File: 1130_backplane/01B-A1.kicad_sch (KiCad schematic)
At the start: 86 parts

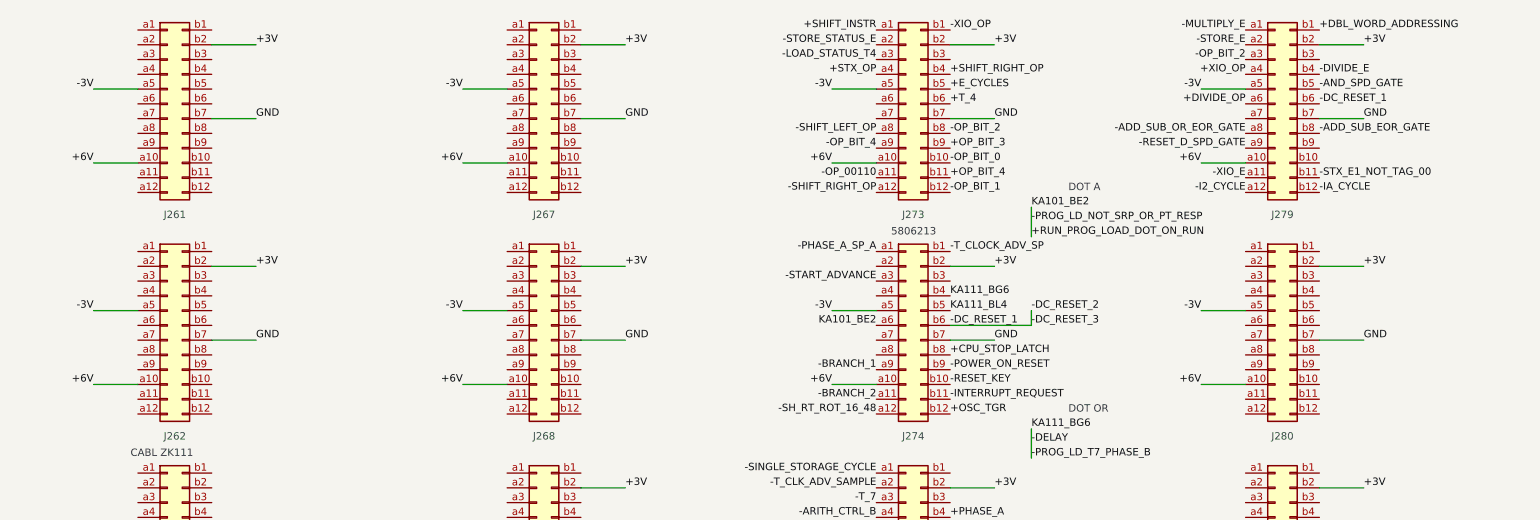
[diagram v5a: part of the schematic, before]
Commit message: Finish page KC101-KC111
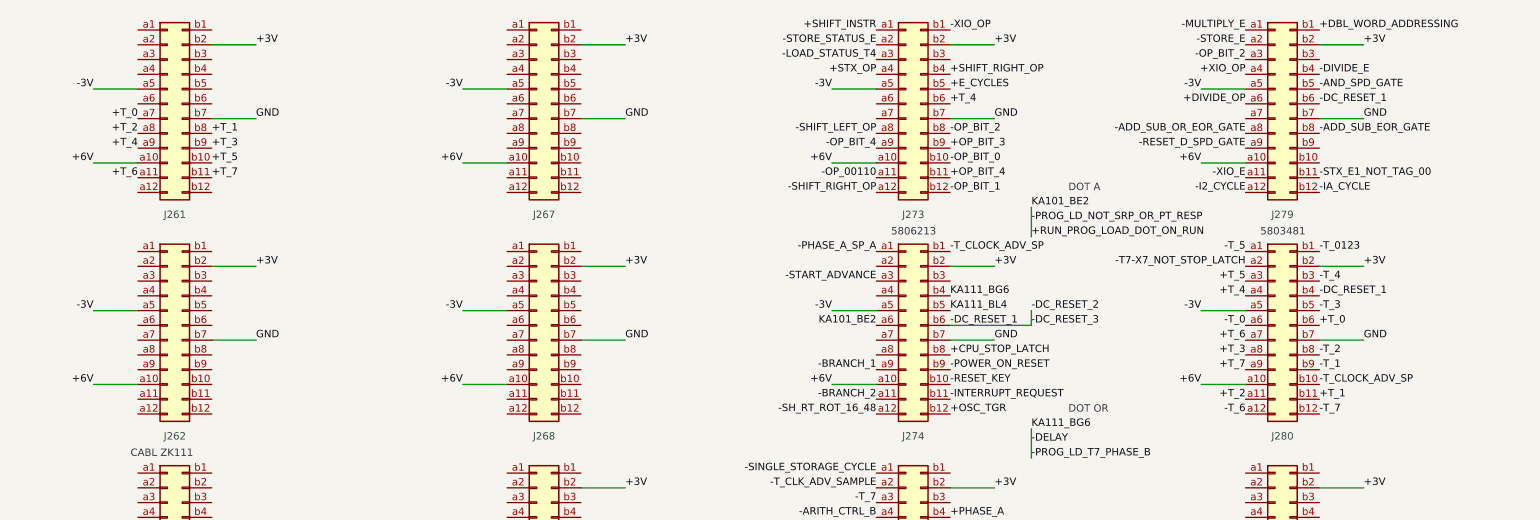
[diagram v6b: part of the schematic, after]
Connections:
- net +T_3: now also J260.b9 (Pin_b9), J279.a8 (Pin_a8)
- net +T_4: now also J260.a9 (Pin_a9), J279.a4 (Pin_a4)
- net +T_5: now also J260.b10 (Pin_b10), J279.a3 (Pin_a3)
- net +T_6: now also J260.a11 (Pin_a11), J279.a7 (Pin_a7)
- net +T_7: now also J260.b11 (Pin_b11), J279.a9 (Pin_a9)
- net -DC_RESET_1: now also J279.b4 (Pin_b4)
- net -T_0: now also J279.a6 (Pin_a6)
- net -T_1: now also J279.b9 (Pin_b9)
- net -T_5: now also J279.a1 (Pin_a1)
- net -T_7: now also J279.b12 (Pin_b12)
- net -T_CLOCK_ADV_SP: now also J279.b10 (Pin_b10)
- net +T_2: now reaches J279.a11 (Pin_a11)
- net +T_2: now also J260.a8 (Pin_a8)
- net -T_6: now reaches J279.a12 (Pin_a12)
- net -T7-X7_NOT_STOP_LATCH: now reaches J279.a2 (Pin_a2)
- net -T_0123: now reaches J279.b1 (Pin_b1)
- net +T_1: now reaches J279.b11 (Pin_b11)
- net +T_1: now also J260.b8 (Pin_b8)
- net -T_4: now reaches J279.b3 (Pin_b3)
- net -T_3: now reaches J279.b5 (Pin_b5)
- net +T_0: now reaches J279.b6 (Pin_b6)
- net +T_0: now also J260.a7 (Pin_a7)
- net -T_2: now reaches J279.b8 (Pin_b8)
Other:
- note added: "5803481"
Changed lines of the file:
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@@
     (effects (font (size 5 5) (thickness 1) bold) (justify left bottom))
+  )
+  (text "5803481" (at 226.06 177.8 0)
+    (effects (font (size 1.27 1.27)) (justify left bottom))
   )
   (text "A" (at 332.74 38.1 0)
@@
     (effects (font (size 1.27 1.27)) (justify right bottom))
   )
+  (label "+T_7" (at 223.52 200.66 180)
+    (effects (font (size 1.27 1.27)) (justify right bottom))
+  )
+  (label "+T_4" (at 223.52 187.96 180)
+    (effects (font (size 1.27 1.27)) (justify right bottom))
+  )
   (label "-PHASE_A_SP_A" (at 160.02 180.34 180)
     (effects (font (size 1.27 1.27)) (justify right bottom))
@@
     (effects (font (size 1.27 1.27)) (justify left bottom))
   )
+  (label "+T_2" (at 33.02 160.02 180)
+    (effects (font (size 1.27 1.27)) (justify right bottom))
+  )
   (label "GND" (at 497.84 157.48 0)
     (effects (font (size 1.27 1.27)) (justify left bottom))
@@
     (effects (font (size 1.27 1.27)) (justify right bottom))
   )
+  (label "-T_4" (at 236.22 185.42 0)
+    (effects (font (size 1.27 1.27)) (justify left bottom))
+  )
   (label "-DC_RESET_1" (at 604.52 104.14 180)
     (effects (font (size 1.27 1.27)) (justify right bottom))
   )
+  (label "-T_6" (at 223.52 208.28 180)
+    (effects (font (size 1.27 1.27)) (justify right bottom))
+  )
   (label "GND" (at 53.34 271.78 0)
     (effects (font (size 1.27 1.27)) (justify left bottom))
@@
     (effects (font (size 1.27 1.27)) (justify left bottom))
   )
+  (label "+T_5" (at 45.72 165.1 0)
+    (effects (font (size 1.27 1.27)) (justify left bottom))
+  )
   (label "+3V" (at 180.34 259.08 0)
     (effects (font (size 1.27 1.27)) (justify left bottom))
@@
     (effects (font (size 1.27 1.27)) (justify right bottom))
   )
+  (label "+T_7" (at 45.72 167.64 0)
+    (effects (font (size 1.27 1.27)) (justify left bottom))
+  )
   (label "-3V" (at 323.85 55.88 180)
     (effects (font (size 1.27 1.27)) (justify right bottom))
@@
     (effects (font (size 1.27 1.27)) (justify left bottom))
   )
+  (label "+T_3" (at 223.52 198.12 180)
+    (effects (font (size 1.27 1.27)) (justify right bottom))
+  )
   (label "+6V" (at 660.4 279.4 180)
     (effects (font (size 1.27 1.27)) (justify right bottom))
@@
     (effects (font (size 1.27 1.27)) (justify left bottom))
   )
+  (label "+T_2" (at 223.52 205.74 180)
+    (effects (font (size 1.27 1.27)) (justify right bottom))
+  )
   (label "-3V" (at 533.4 266.7 180)
     (effects (font (size 1.27 1.27)) (justify right bottom))
@@
     (effects (font (size 1.27 1.27)) (justify left bottom))
   )
+  (label "-T_2" (at 236.22 198.12 0)
+    (effects (font (size 1.27 1.27)) (justify left bottom))
+  )
   (label "-INTERRUPT_LVLS_45" (at 553.72 266.7 0)
     (effects (font (size 1.27 1.27)) (justify left bottom))
@@
     (effects (font (size 1.27 1.27)) (justify right bottom))
   )
+  (label "+T_6" (at 223.52 195.58 180)
+    (effects (font (size 1.27 1.27)) (justify right bottom))
+  )
   (label "+PHASE_B" (at 604.52 142.24 180)
     (effects (font (size 1.27 1.27)) (justify right bottom))
@@
     (effects (font (size 1.27 1.27)) (justify left bottom))
   )
+  (label "-T_0" (at 223.52 193.04 180)
+    (effects (font (size 1.27 1.27)) (justify right bottom))
+  )
   (label "KA101_AA5" (at 287.02 226.06 180)
     (effects (font (size 1.27 1.27)) (justify right bottom))
@@
     (effects (font (size 1.27 1.27)) (justify left bottom))
   )
+  (label "-T_CLOCK_ADV_SP" (at 236.22 203.2 0)
+    (effects (font (size 1.27 1.27)) (justify left bottom))
+  )
   (label "+SHIFT_RIGHT_OP" (at 172.72 149.86 0)
     (effects (font (size 1.27 1.27)) (justify left bottom))
@@
     (effects (font (size 1.27 1.27)) (justify left bottom))
   )
+  (label "+T_4" (at 33.02 162.56 180)
+    (effects (font (size 1.27 1.27)) (justify right bottom))
+  )
   (label "+3V" (at 243.84 297.18 0)
     (effects (font (size 1.27 1.27)) (justify left bottom))
@@
     (effects (font (size 1.27 1.27)) (justify right bottom))
   )
+  (label "-T_3" (at 236.22 190.5 0)
+    (effects (font (size 1.27 1.27)) (justify left bottom))
+  )
   (label "+SINGLE_STEP_MODE" (at 45.72 248.92 0)
     (effects (font (size 1.27 1.27)) (justify left bottom))
@@
     (effects (font (size 1.27 1.27)) (justify right bottom))
   )
+  (label "-T_0123" (at 236.22 180.34 0)
+    (effects (font (size 1.27 1.27)) (justify left bottom))
+  )
   (label "+E2_CYCLE" (at 477.52 297.18 180)
     (effects (font (size 1.27 1.27)) (justify right bottom))
@@
     (effects (font (size 1.27 1.27)) (justify left bottom))
   )
+  (label "-T_5" (at 223.52 180.34 180)
+    (effects (font (size 1.27 1.27)) (justify right bottom))
+  )
   (label "KA101_AA3" (at 287.02 223.52 180)
     (effects (font (size 1.27 1.27)) (justify right bottom))
@@
     (effects (font (size 1.27 1.27)) (justify left bottom))
   )
+  (label "+T_1" (at 236.22 205.74 0)
+    (effects (font (size 1.27 1.27)) (justify left bottom))
+  )
   (label "DN201_AE4" (at 490.22 299.72 0)
     (effects (font (size 1.27 1.27)) (justify left bottom))
@@
     (effects (font (size 1.27 1.27)) (justify right bottom))
   )
+  (label "-T_7" (at 236.22 208.28 0)
+    (effects (font (size 1.27 1.27)) (justify left bottom))
+  )
   (label "-CS_LEVELS" (at 617.22 276.86 0)
     (effects (font (size 1.27 1.27)) (justify left bottom))
@@
     (effects (font (size 1.27 1.27)) (justify right bottom))
   )
+  (label "+T_5" (at 223.52 185.42 180)
+    (effects (font (size 1.27 1.27)) (justify right bottom))
+  )
   (label "+BR_OR_SKIP_ON_COND" (at 160.02 119.38 180)
     (effects (font (size 1.27 1.27)) (justify right bottom))
@@
     (effects (font (size 1.27 1.27)) (justify left bottom))
   )
+  (label "-DC_RESET_1" (at 236.22 187.96 0)
+    (effects (font (size 1.27 1.27)) (justify left bottom))
+  )
   (label "-3V" (at 469.9 190.5 180)
     (effects (font (size 1.27 1.27)) (justify right bottom))
@@
     (effects (font (size 1.27 1.27)) (justify left bottom))
   )
+  (label "+T_3" (at 45.72 162.56 0)
+    (effects (font (size 1.27 1.27)) (justify left bottom))
+  )
   (label "GND" (at 688.34 309.88 0)
     (effects (font (size 1.27 1.27)) (justify left bottom))
@@
     (effects (font (size 1.27 1.27)) (justify right bottom))
   )
+  (label "-T7-X7_NOT_STOP_LATCH" (at 223.52 182.88 180)
+    (effects (font (size 1.27 1.27)) (justify right bottom))
+  )
   (label "+6V" (at 596.9 317.5 180)
     (effects (font (size 1.27 1.27)) (justify right bottom))
@@
     (effects (font (size 1.27 1.27)) (justify left bottom))
   )
+  (label "+T_0" (at 236.22 193.04 0)
+    (effects (font (size 1.27 1.27)) (justify left bottom))
+  )
   (label "+T_5" (at 604.52 170.18 180)
     (effects (font (size 1.27 1.27)) (justify right bottom))
@@
     (effects (font (size 1.27 1.27)) (justify right bottom))
   )
+  (label "-T_1" (at 236.22 200.66 0)
+    (effects (font (size 1.27 1.27)) (justify left bottom))
+  )
   (label "-3V" (at 723.9 304.8 180)
     (effects (font (size 1.27 1.27)) (justify right bottom))
@@
     (effects (font (size 1.27 1.27)) (justify right bottom))
   )
+  (label "+T_1" (at 45.72 160.02 0)
+    (effects (font (size 1.27 1.27)) (justify left bottom))
+  )
   (label "-3V" (at 596.9 114.3 180)
     (effects (font (size 1.27 1.27)) (justify right bottom))
@@
     (effects (font (size 1.27 1.27)) (justify left bottom))
   )
+  (label "+T_6" (at 33.02 167.64 180)
+    (effects (font (size 1.27 1.27)) (justify right bottom))
+  )
   (label "GND" (at 561.34 195.58 0)
     (effects (font (size 1.27 1.27)) (justify left bottom))
@@
     (effects (font (size 1.27 1.27)) (justify right bottom))
   )
+  (label "+T_0" (at 33.02 157.48 180)
+    (effects (font (size 1.27 1.27)) (justify right bottom))
+  )

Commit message: Finish page KD101-KD111
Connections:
- net +E1_CYCLE: now also J260.b1 (Pin_b1), J299.b5 (Pin_b5)
- net +E2_CYCLE: now also J260.b3 (Pin_b3), J299.a7 (Pin_a7)
- net +E_CYCLES: now also J299.b8 (Pin_b8)
- net +FORMAT_5: now also J300.b9 (Pin_b9)
- net +I1_T4: now also J299.a11 (Pin_a11)
- net +T_2: now also J300.a7 (Pin_a7)
- net +T_3: now also J299.b6 (Pin_b6)
- net +T_4: now also J299.b10 (Pin_b10)
- net -DC_RESET_1: now also J299.a2 (Pin_a2)
- net -E_GT_TURN_ON: now also J299.b11 (Pin_b11)
- net -I1_T4: now also J299.a12 (Pin_a12)
- net -I2_CYCLE: now also J300.b1 (Pin_b1)
- net -IA_CYCLE: now also J299.a9 (Pin_a9)
- net -INDEX_INSTR: now also J300.b12 (Pin_b12)
- net -XIO_E2_R_W: now also J299.a8 (Pin_a8)
- net +I1_CYCLE: now reaches J260.a1 (Pin_a1)
- net +I1_CYCLE: now also J300.b8 (Pin_b8)
- net +I2_CYCLE: now reaches J260.a2 (Pin_a2)
- net +I2_CYCLE: now also J300.a4 (Pin_a4), J344.a3 (Pin_a3)
- net +IA_CYCLE: now reaches J260.a3 (Pin_a3)
- net +IA_CYCLE: now also J299.b12 (Pin_b12)
- net +IX_CYCLE: now reaches J260.a4 (Pin_a4)
- net +IX_CYCLE: now also J300.a3 (Pin_a3)
- net +E3_CYCLE: now reaches J260.b4 (Pin_b4)
- net +E3_CYCLE: now also J299.b3 (Pin_b3)
- net +I1_T3: now reaches J299.a3 (Pin_a3)
- net +E_GT_TURN_ON: now reaches J299.a4 (Pin_a4)
- net -E_CYCLES: now reaches J299.a6 (Pin_a6)
- net -LOAD_DISPLAY_PROGRAM_LOAD: now reaches J299.b9 (Pin_b9)
- net +I1_POWERED: now reaches J344.a2 (Pin_a2)
- net +I1_POWERED: now also J300.b11 (Pin_b11)
- net +GT_B_BITS_0_TO_9_TO_OP_REG: now reaches J340.a9 (Pin_a9)
- net +GT_B_BITS_0_TO_9_TO_OP_REG: now also J300.b5 (Pin_b5)
- net -IX_CYCLE: now reaches J300.a1 (Pin_a1)
- net +MOD_8: now reaches J300.a11 (Pin_a11)
- net -I1_CYCLE: now reaches J300.a12 (Pin_a12)
- net -NOT_END_OP_TO_SP: now reaches J300.a2 (Pin_a2)
- net -TAG_00: now reaches J300.a8 (Pin_a8)
- net -END_OP_TO_SP: now reaches J300.a9 (Pin_a9)
- net -IX_GT_TURN_ON: now reaches J300.b3 (Pin_b3)
- net -SHIFT_INSTR: now reaches J300.b6 (Pin_b6)
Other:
- note added: "5804672"

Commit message: Finish page KG101-KG151
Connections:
- net -I_O_TO_B_SP_0-7: now reaches J341.a8 (Pin_a8)
- net -RESET_D_REG_SP: now reaches J340.b3 (Pin_b3)
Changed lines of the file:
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@@
+    (effects (font (size 1.27 1.27)) (justify right bottom))
+  )
+  (label "-I_O_TO_B_SP_0-7" (at 795.02 198.12 180)
     (effects (font (size 1.27 1.27)) (justify right bottom))
   )
@@
     (effects (font (size 1.27 1.27)) (justify right bottom))
   )
+  (label "-RESET_D_REG_SP" (at 807.72 147.32 0)
+    (effects (font (size 1.27 1.27)) (justify left bottom))
+  )
   (label "GND" (at 815.34 119.38 0)
